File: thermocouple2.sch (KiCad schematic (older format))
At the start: 2 parts

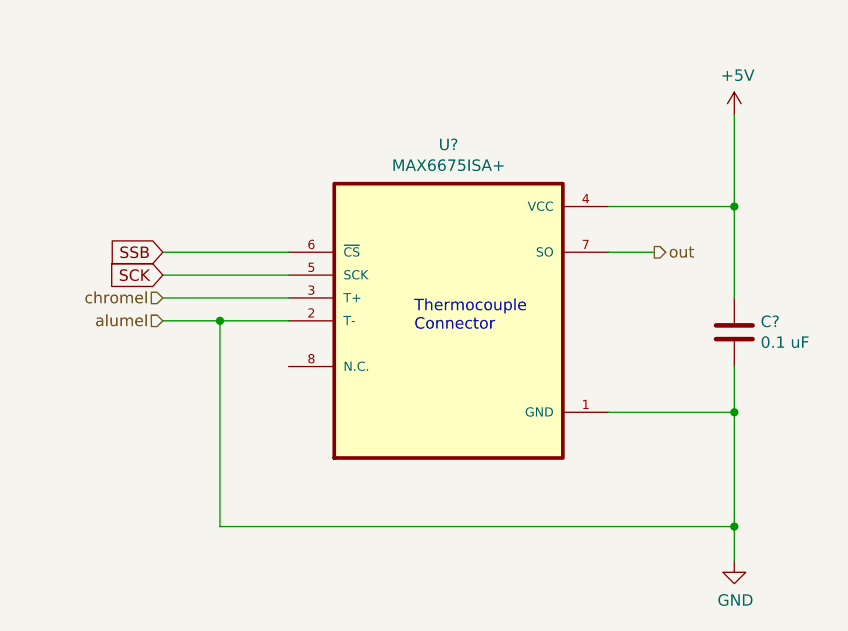
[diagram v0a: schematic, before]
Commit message: updated SCK
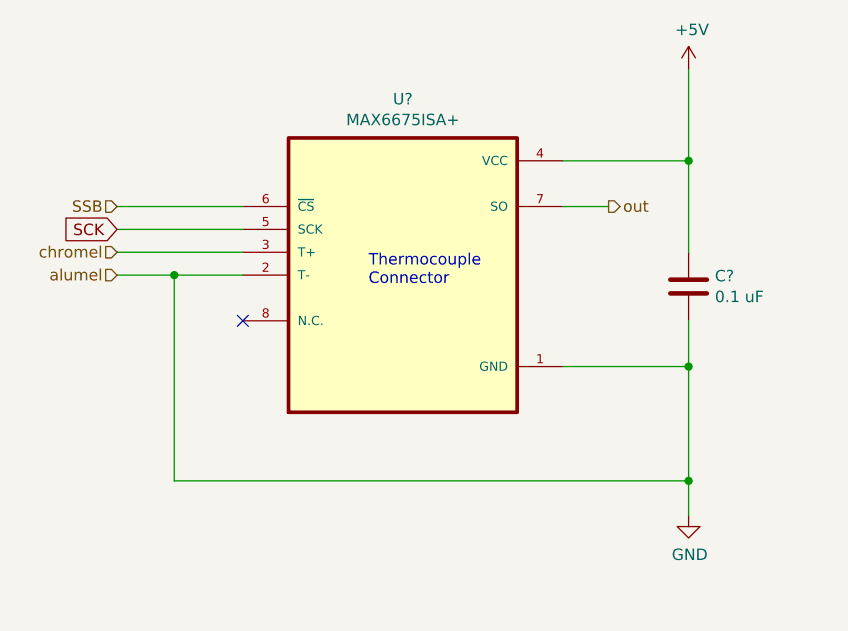
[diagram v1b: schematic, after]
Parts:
- removed C?: 0.1 uF, symbol Device:C
- removed U?: MAX6675ISA+, SOIC127P600X175-8N, symbol MAX6675ISA_:MAX6675ISA+
- added C?: 0.1 uF, symbol Device:C
- added U?: MAX6675ISA+, SOIC127P600X175-8N, symbol MAX6675ISA_:MAX6675ISA+
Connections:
- net +5V: now also C?.1, U?.4 (VCC)
- net GND: now also C?.2, U?.1 (GND), U?.2 (T-)
- net SCK: now also U?.5 (SCK)
- net SSB: now also U?.6 (~CS)
- net chromel: now also U?.3 (T+)
- net out: now also U?.7 (SO)
- no-connect marks 0 -> 1
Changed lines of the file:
@@
 Comment4 ""
 $EndDescr
-Text GLabel 4350 3400 0    50   Input ~ 0
-SCK
-Text GLabel 4350 3300 0    50   Input ~ 0
-SSB
-Connection ~ 6850 4000
+Connection ~ 6650 3800
 $Comp
 L MAX6675ISA_:MAX6675ISA+ U?
-U 1 1 604DC823
-P 5600 3600
-F 0 "U?" H 5600 4370 50  0000 C CNN
-F 1 "MAX6675ISA+" H 5600 4279 50  0000 C CNN
-F 2 "SOIC127P600X175-8N" H 5600 3600 50  0001 L BNN
-F 3 "" H 5600 3600 50  0001 L BNN
-	1    5600 3600
+U 1 1 605103AB
+P 5400 3400
+F 0 "U?" H 5400 4170 50  0000 C CNN
+F 1 "MAX6675ISA+" H 5400 4079 50  0000 C CNN
+F 2 "SOIC127P600X175-8N" H 5400 3400 50  0001 L BNN
+F 3 "" H 5400 3400 50  0001 L BNN
+	1    5400 3400
 	1    0    0    -1
 $EndComp
 Wire Wire Line
-	6850 4000 6850 4500
+	6650 3800 6650 4300
 Wire Wire Line
-	4600 4500 4600 3600
+	4400 4300 4400 3400
 Wire Wire Line
-	4600 3600 4900 3600
-Text Notes 5450 3650 0    50   ~ 0
+	4400 3400 4700 3400
+Text Notes 5250 3450 0    50   ~ 0
 Thermocouple\nConnector
 Wire Wire Line
-	4350 3600 4600 3600
-Connection ~ 4600 3600
+	4150 3400 4400 3400
+Connection ~ 4400 3400
 Wire Wire Line
-	4900 3500 4350 3500
+	4700 3300 4150 3300
 Wire Wire Line
-	6300 3100 6850 3100
+	6100 2900 6650 2900
 Wire Wire Line
-	6300 4000 6850 4000
+	6100 3800 6650 3800
 Wire Wire Line
-	4600 4500 6850 4500
+	4400 4300 6650 4300
 Wire Wire Line
-	6300 3300 6500 3300
+	6100 3100 6300 3100
 Wire Wire Line
-	4350 3400 4900 3400
+	4150 3200 4700 3200
 Wire Wire Line
-	4900 3300 4350 3300
+	4700 3100 4150 3100
 Wire Wire Line
-	6850 3100 6850 2700
-Connection ~ 6850 3100
+	6650 2900 6650 2500
+Connection ~ 6650 2900
 Wire Wire Line
-	6850 4500 6850 4650
-Connection ~ 6850 4500
+	6650 4300 6650 4450
+Connection ~ 6650 4300
 $Comp
 L power:GND #PWR?
-U 1 1 604DC83A
-P 6850 4650
-F 0 "#PWR?" H 6850 4400 50  0001 C CNN
-F 1 "GND" H 6855 4477 50  0000 C CNN
-F 2 "" H 6850 4650 50  0001 C CNN
-F 3 "" H 6850 4650 50  0001 C CNN
-	1    6850 4650
+U 1 1 605103C2
+P 6650 4450
+F 0 "#PWR?" H 6650 4200 50  0001 C CNN
+F 1 "GND" H 6655 4277 50  0000 C CNN
+F 2 "" H 6650 4450 50  0001 C CNN
+F 3 "" H 6650 4450 50  0001 C CNN
+	1    6650 4450
 	1    0    0    -1
 $EndComp
 $Comp
 L power:+5V #PWR?
-U 1 1 604DC840
-P 6850 2700
-F 0 "#PWR?" H 6850 2550 50  0001 C CNN
-F 1 "+5V" H 6865 2873 50  0000 C CNN
-F 2 "" H 6850 2700 50  0001 C CNN
-F 3 "" H 6850 2700 50  0001 C CNN
-	1    6850 2700
+U 1 1 605103C8
+P 6650 2500
+F 0 "#PWR?" H 6650 2350 50  0001 C CNN
+F 1 "+5V" H 6665 2673 50  0000 C CNN
+F 2 "" H 6650 2500 50  0001 C CNN
+F 3 "" H 6650 2500 50  0001 C CNN
+	1    6650 2500
 	1    0    0    -1
 $EndComp
 $Comp
 L Device:C C?
-U 1 1 604DC846
-P 6850 3650
-F 0 "C?" H 6965 3696 50  0000 L CNN
-F 1 "0.1 uF" H 6965 3605 50  0000 L CNN
-F 2 "" H 6888 3500 50  0001 C CNN
-F 3 "~" H 6850 3650 50  0001 C CNN
-	1    6850 3650
+U 1 1 605103CE
+P 6650 3450
+F 0 "C?" H 6765 3496 50  0000 L CNN
+F 1 "0.1 uF" H 6765 3405 50  0000 L CNN
+F 2 "" H 6688 3300 50  0001 C CNN
+F 3 "~" H 6650 3450 50  0001 C CNN
+	1    6650 3450
 	1    0    0    -1
 $EndComp
 Wire Wire Line
-	6850 3100 6850 3500
+	6650 2900 6650 3300
 Wire Wire Line
-	6850 3800 6850 4000
-Text HLabel 6500 3300 2    50   Output ~ 0
+	6650 3600 6650 3800
+Text HLabel 6300 3100 2    50   Output ~ 0
 out
-Text HLabel 4350 3500 0    50   Input ~ 0
+Text HLabel 4150 3300 0    50   Input ~ 0
 chromel
-Text HLabel 4350 3600 0    50   Input ~ 0
+Text HLabel 4150 3400 0    50   Input ~ 0
 alumel
+Text HLabel 4150 3100 0    50   Input ~ 0
+SSB
+NoConn ~ 4700 3600
+Text GLabel 4150 3200 0    50   Input ~ 0
+SCK
 $EndSCHEMATC
